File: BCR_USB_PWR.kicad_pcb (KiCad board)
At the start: 2 copper layers, 21.8 x 13.2 mm, 2 parts, among them CN1 DB9_Female, CN2 UE27AC54100

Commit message: clean up junk files
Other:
- board text removed: "100/200"
- board text removed: "TRS-80 Model 100 / TANDY 200"
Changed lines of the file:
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@@
   (general
     (thickness 1.6)
-    (drawings 19)
+    (drawings 17)
     (tracks 4)
     (zones 0)
@@
     )
   )
-  (gr_text 100/200 (at 121.3 90.458) (layer F.SilkS)
-    (effects (font (size 0.8 0.8) (thickness 0.1)))
-  )
   (gr_line (start 136.6 90.408) (end 136.6 101.108) (layer Dwgs.User) (width 0.15))
   (gr_line (start 117.4 90.408) (end 136.6 90.408) (layer Dwgs.User) (width 0.15))
@@
     (effects (font (size 0.6 0.6) (thickness 0.1)) (justify mirror))
   )
-  (gr_text "TRS-80 Model 100 / TANDY 200" (at 125.7 91.058) (layer B.SilkS)
-    (effects (font (size 0.6 0.6) (thickness 0.1)) (justify mirror))
-  )

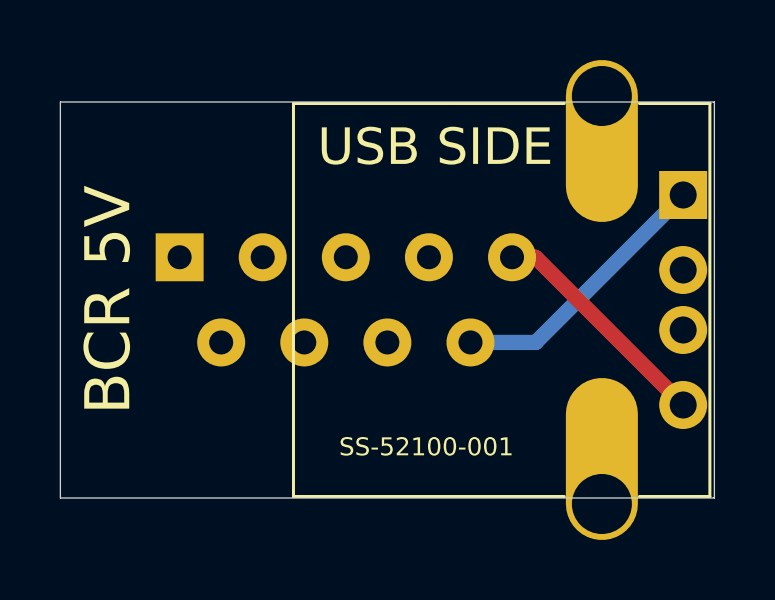
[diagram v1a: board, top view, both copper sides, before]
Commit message: rename NEC to up_long, and a short up version that covers up the shorting hazard
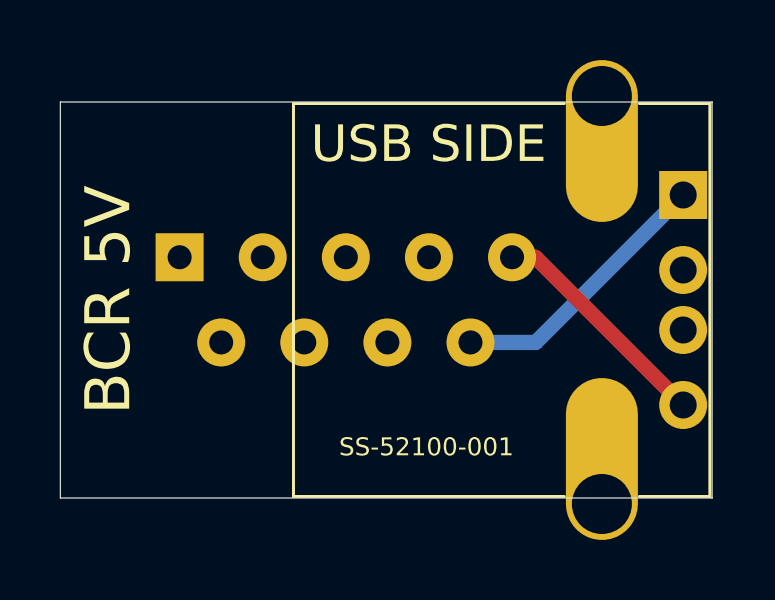
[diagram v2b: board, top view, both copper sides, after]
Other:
- board size 21.8 x 13.2 mm -> 21.7 x 13.2 mm
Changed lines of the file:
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@@
     (effects (font (size 1.2192 1.2192) (thickness 0.2032)) (justify mirror))
   )
-  (gr_text "USB SIDE" (at 130 90.658) (layer F.SilkS)
+  (gr_text "USB SIDE" (at 129.775 90.558) (layer F.SilkS)
     (effects (font (size 1.2192 1.2192) (thickness 0.2032)))
   )
   (gr_line (start 117.5 89.158) (end 117.5 102.358) (layer Edge.Cuts) (width 0.0254))
-  (gr_line (start 139.3 89.158) (end 117.5 89.158) (layer Edge.Cuts) (width 0.0254))
-  (gr_line (start 139.3 102.358) (end 139.3 89.158) (layer Edge.Cuts) (width 0.0254))
-  (gr_line (start 117.5 102.358) (end 139.3 102.358) (layer Edge.Cuts) (width 0.0254))
+  (gr_line (start 139.225 89.158) (end 117.5 89.158) (layer Edge.Cuts) (width 0.0254))
+  (gr_line (start 139.225 102.358) (end 139.225 89.158) (layer Edge.Cuts) (width 0.0254))
+  (gr_line (start 117.5 102.358) (end 139.225 102.358) (layer Edge.Cuts) (width 0.0254))
   (segment (start 133.345 97.173) (end 131.17 97.173) (width 0.508) (layer B.Cu) (net 1))
   (segment (start 138.26 92.258) (end 133.345 97.173) (width 0.508) (layer B.Cu) (net 1))
